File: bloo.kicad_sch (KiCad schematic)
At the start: 89 parts, among them J5 SWD_Header, M1 M1_Conn_Alt, M2 M2_Conn_Alt, Q0 TEFT4300, Q1 TEFT4300, Q10 Q_NMOS_GSD, Q11 Q_NMOS_GSD, Q12 Q_NMOS_GSD, Q2 TEFT4300, Q3 TEFT4300, Q9 Q_NMOS_GSD, SW1 SW, SW2 SW, SW3 SW, U1 YAAJ_BluePill_SWD_Breakout, U2 L293D, U3 LM1085-5.0, U4 APE8865Y5-33-HF-3, U5 BC832

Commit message: BOM Complete
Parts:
- BT1: LCSC Part # (none) -> C160262
- C1, C12, C13, C19, C4: LCSC Part # (none) -> C600013
- C10: LCSC Part # (none) -> C1952791
- C11, C9: LCSC Part # (none) -> C39127
- C14, C15, C17, C18, C20, C21, C3: LCSC Part # (none) -> C28322
- C16, C2: LCSC Part # (none) -> C1590882
- C25: LCSC Part # (none) -> C1846
- C5: LCSC Part # (none) -> C1590
- C6: LCSC Part # (none) -> C140782
- D0, D1, D2, D3: LCSC Part # (none) -> C2900370
- D4: LCSC Part # (none) -> C5879380
- D5: LCSC Part # (none) -> C2890404
- D6: LCSC Part # (none) -> C2293
- L1: LCSC Part # (none) -> C845121
- M1, M2: LCSC Part # (none) -> C144397
- Q0, Q1, Q2, Q3: LCSC Part # (none) -> C118301
- Q10, Q11, Q12, Q9: LCSC Part # (none) -> C5310967
- R1, R2, R3, R4: value 1.8k -> 1.8K; LCSC Part # (none) -> C22108
- R10: value 10k -> 10K; LCSC Part # (none) -> C2479071
- R11, R12, R13, R14, R15, R16, R24: LCSC Part # (none) -> C25664
- R19: LCSC Part # (none) -> C17985
- R20, R21: LCSC Part # (none) -> C17987
- R22: LCSC Part # (none) -> C18003
- R23, R9: LCSC Part # (none) -> C2479751
- R5, R6, R7, R8: value 35 -> 36; LCSC Part # (none) -> C18006
- S1: LCSC Part # (none) -> C6689036
- SW1, SW2, SW3, SW_RST1: LCSC Part # (none) -> C2801245
- U1: LCSC Part # (none) -> C22396880; now not fitted
- U2: LCSC Part # (none) -> C12340
- U3: LCSC Part # (none) -> C129950
- U4: value APE8865Y5-33-HF-3 -> NCP161ASN330T1G; LCSC Part # (none) -> C892187
- U5: now not fitted

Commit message: Started Reza's suggested changes
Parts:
- removed R11: 47K, Resistor_SMD:R_1206_3216Metric_Pad1.30x1.75mm_HandSolder, symbol Device:R
- removed SW1: SW, Button_Switch_SMD:SW_SPST_REED_CT05-XXXX-G1, symbol Switch:SW_Push
- added C22: 0.1uF, Capacitor_SMD:C_1206_3216Metric_Pad1.33x1.80mm_HandSolder, symbol Device:C
- added C7, C8: 12pF, symbol Device:C
- added D7, D9: 1SS389,L3F, Diode_SMD:D_SOD-523, symbol Diode:1N4148WT
- added R17: 47K, Resistor_SMD:R_1206_3216Metric_Pad1.30x1.75mm_HandSolder, symbol Device:R
- added Y1: ABS07-32.768KHZ-T, AS07-XTAL:XTAL_ABS07-32.768KHZ-T, symbol ABS07-XTAL:ABS07-32.768KHZ-T
- BT1: footprint Connector_PinSocket_2.54mm:PinSocket_1x02_P2.54mm_Vertical -> Connector_JST:JST_EH_B2B-EH-A_1x02_P2.50mm_Vertical
- U1, U5: now fitted
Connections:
- net BUTTON is gone; now on net BLE_SPI_MISO: U1.12 (PB4)
- net +3V3: now also M1.4 (Pin_4), M2.4 (Pin_4), R17.2; no longer M1.3 (Pin_3), M2.3 (Pin_3)
- net BLE_STATE: now also U5.D2 (P19); no longer U5.2 (P20/LED)
- net BT_RESET: now also C22.1, D9.2 (A), R17.1
- net EMIT_4: now also U1.22 (PC13); no longer U1.13 (PB5)
- net GND: now also C19.1, M1.1 (Pin_1), M2.1 (Pin_1), C22.2, C7.1, C8.1; no longer C19.2, M1.6 (Pin_6), M2.6 (Pin_6)
- net M1_ENC_A: now also M1.3 (Pin_3); no longer M2.4 (Pin_4)
- net M1_ENC_B: now also M1.2 (Pin_2); no longer M2.5 (Pin_5)
- net M1_OUT_1: now also M1.6 (Pin_6); no longer M2.1 (Pin_1)
- net M1_OUT_2: now also M1.5 (Pin_5); no longer M2.2 (Pin_2)
- net M2_ENC_A: now also M2.3 (Pin_3); no longer M1.4 (Pin_4)
- net M2_ENC_B: now also M2.2 (Pin_2); no longer M1.5 (Pin_5)
- net M2_OUT_1: now also M2.6 (Pin_6); no longer M1.1 (Pin_1)
- net M2_OUT_2: now also M2.5 (Pin_5); no longer M1.2 (Pin_2)
- net RST: now also C19.2, D7.2 (A); no longer C19.1, SW_RST1.1
- net BLE_SPI_SCK: now reaches U1.11 (PB3)
- net BLE_SPI_SCK: now also U5.A5 (P08)
- net BLE_LED: now reaches U1.24 (PC15)
- net BLE_LED: now also U5.A2 (P17)
- net at U5.11 (P00/XL1): now also C8.2, Y1.1
- net at U5.12 (P01/XL2): now also C7.2, Y1.2
- net BLE_SPI_MISO: now reaches U5.C5 (P09)
- net BLE_SPI_MOSI: now reaches U5.D5 (P10)
- net BLE_SPI_MOSI: now also U1.13 (PB5)
- new net: D7.1 (K), D9.1 (K), SW_RST1.1
- no-connect marks 32 -> 24
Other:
- moved on the sheet: C19, J5, M1, M2, R12, R24, R9, SW2, SW3, SW_RST1

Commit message: updated button footprint
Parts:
- SW3: footprint Button_Switch_SMD:SW_SPST_REED_CT05-XXXX-G1 -> MM_Library:SW4_SKRPABE010_ALPS
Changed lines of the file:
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@@
 			)
 		)
-		(property "Footprint" "Button_Switch_SMD:SW_SPST_REED_CT05-XXXX-G1"
+		(property "Footprint" "MM_Library:SW4_SKRPABE010_ALPS"
 			(at 46.355 252.73 0)
 			(effects

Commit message: reorganized schematics
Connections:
- net BUTTON_3 is gone; now on net BUTTON_2: R9.2, SW3.1, U1.17 (PB9)
- net BUTTON_2: no longer R24.2, SW2.1, U1.23 (PC14)
- new net BUTTON: R24.2, SW2.1, U1.23 (PC14)
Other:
- note added: "Buttons"
- note added: "LEDs"
- note removed: "Button, LEDs"
- moved on the sheet: BT1, BT_MH1, BT_MH2, BT_MH3, BT_MH4, C1, C10, C11, C12, C13, C14, C15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

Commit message: updated pcb from schematics
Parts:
- C7, C8: footprint (none) -> Capacitor_SMD:C_0603_1608Metric_Pad1.08x0.95mm_HandSolder
- Y1: footprint AS07-XTAL:XTAL_ABS07-32.768KHZ-T -> MM_Library:CAP_ABS07-32.768KHZ-T_ABR
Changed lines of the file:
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@@
 			)
 		)
-		(property "Footprint" ""
+		(property "Footprint" "Capacitor_SMD:C_0603_1608Metric_Pad1.08x0.95mm_HandSolder"
 			(at 295.91 137.4648 0)
 			(effects
@@
 			)
 		)
-		(property "Footprint" ""
+		(property "Footprint" "Capacitor_SMD:C_0603_1608Metric_Pad1.08x0.95mm_HandSolder"
 			(at 295.91 124.7648 0)
 			(effects
@@
 			)
 		)
-		(property "Footprint" "AS07-XTAL:XTAL_ABS07-32.768KHZ-T"
+		(property "Footprint" "MM_Library:CAP_ABS07-32.768KHZ-T_ABR"
 			(at 299.72 132.08 0)
 			(effects

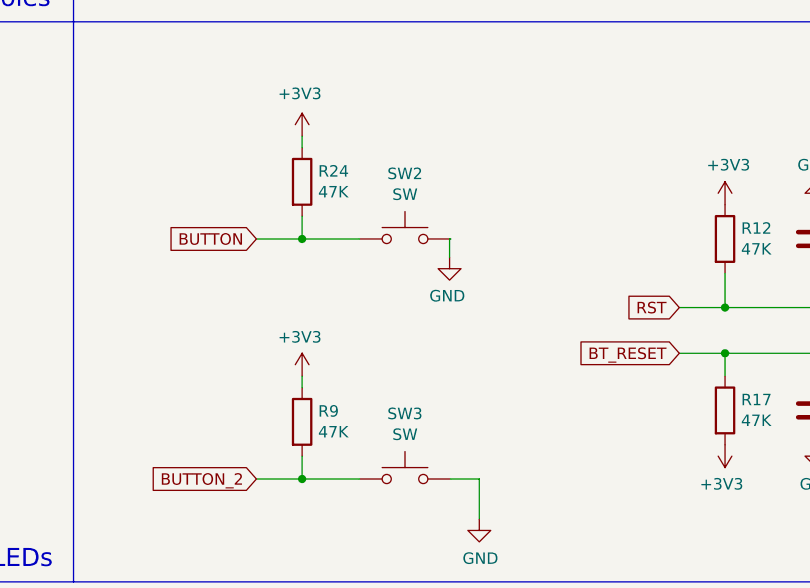
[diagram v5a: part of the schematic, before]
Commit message: updated buttons in pcb
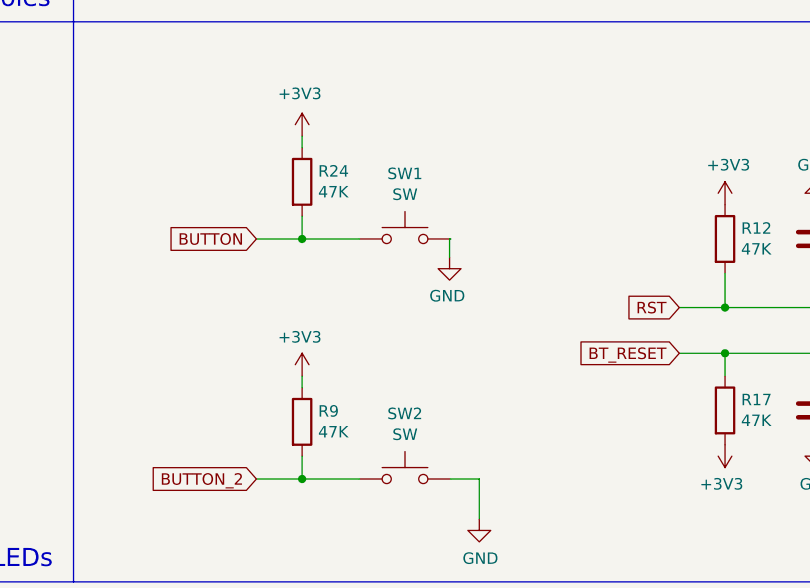
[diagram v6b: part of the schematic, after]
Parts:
- SW1: renamed from SW2; footprint Button_Switch_SMD:SW_SPST_REED_CT05-XXXX-G1 -> MM_Library:SW4_SKRPABE010_ALPS
- SW_RST1: footprint Button_Switch_SMD:SW_SPST_REED_CT05-XXXX-G1 -> MM_Library:SW4_SKRPABE010_ALPS
- U5: footprint custom_foot:XCVR_BC832 -> MM_Library:XCVR_BC832
- renumbered SW3 to SW2
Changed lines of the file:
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@@
 			)
 		)
-		(property "Footprint" "Button_Switch_SMD:SW_SPST_REED_CT05-XXXX-G1"
+		(property "Footprint" "MM_Library:SW4_SKRPABE010_ALPS"
 			(at 388.62 212.09 0)
 			(effects
@@
 		(on_board yes)
 		(dnp no)
-		(property "Reference" "SW2"
+		(property "Reference" "SW1"
 			(at 303.53 202.311 0)
 			(effects
@@
 			)
 		)
-		(property "Footprint" "Button_Switch_SMD:SW_SPST_REED_CT05-XXXX-G1"
+		(property "Footprint" "MM_Library:SW4_SKRPABE010_ALPS"
 			(at 303.53 204.47 0)
 			(effects
@@
 			(project "bloo"
 				(path "/9031bb33-c6aa-4758-bf5c-3274ed3ebab7"
-					(reference "SW2")
+					(reference "SW1")
 					(unit 1)
 				)
@@
 			)
 		)
-		(property "Footprint" "custom_foot:XCVR_BC832"
+		(property "Footprint" "MM_Library:XCVR_BC832"
 			(at 347.98 146.05 0)
 			(effects
@@
 		(on_board yes)
 		(dnp no)
-		(property "Reference" "SW3"
+		(property "Reference" "SW2"
 			(at 303.53 228.981 0)
 			(effects
@@
 			(project "bloo"
 				(path "/9031bb33-c6aa-4758-bf5c-3274ed3ebab7"
-					(reference "SW3")
+					(reference "SW2")
 					(unit 1)
 				)

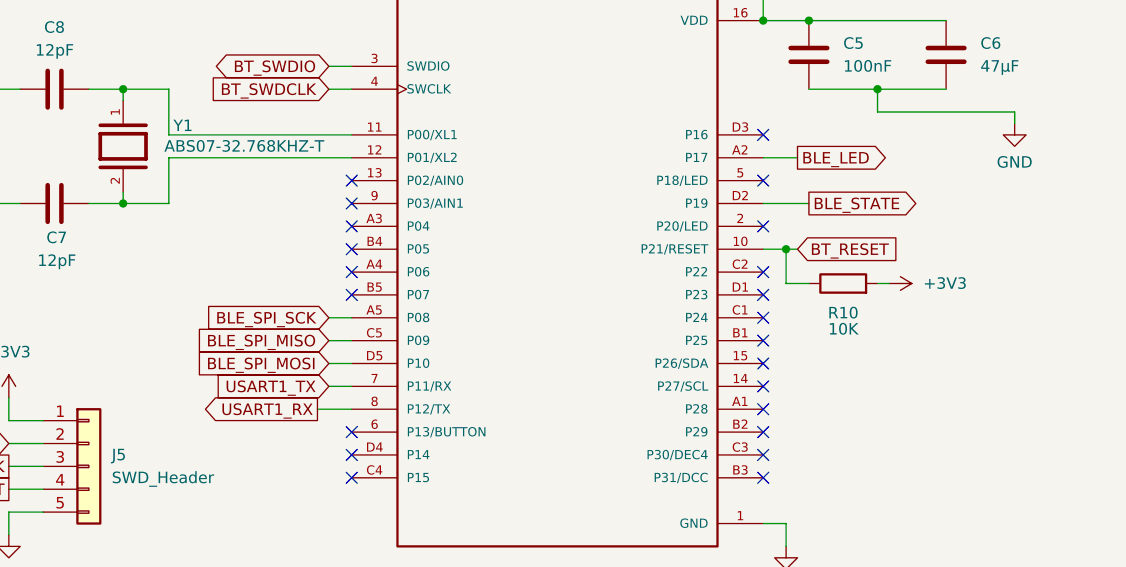
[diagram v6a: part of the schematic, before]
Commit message: change bluetooth SPI pins
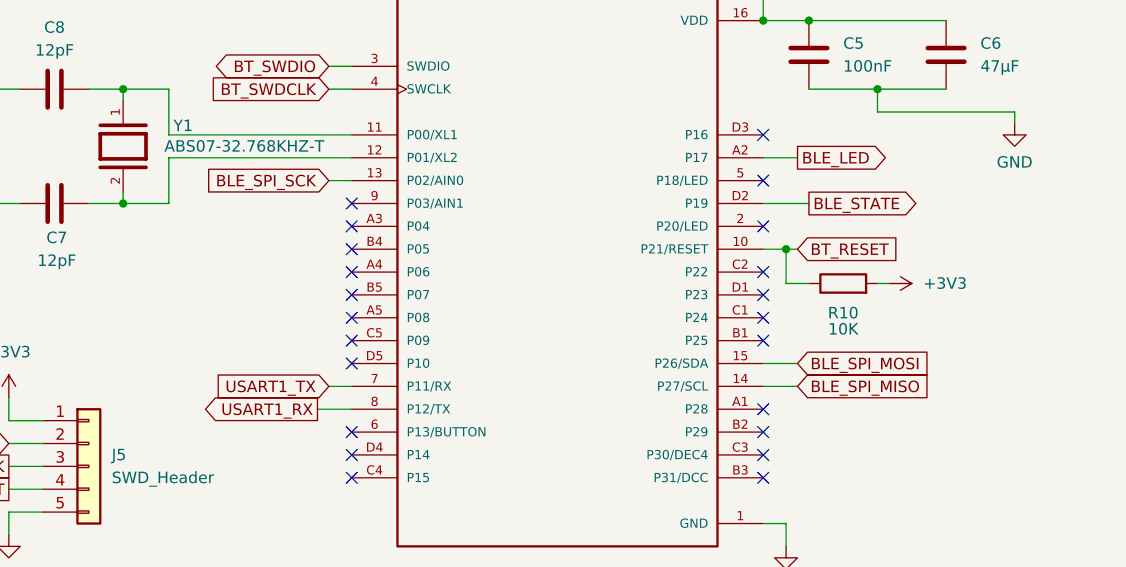
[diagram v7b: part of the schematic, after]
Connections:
- net BLE_SPI_MISO: now also U5.14 (P27/SCL); no longer U5.C5 (P09)
- net BLE_SPI_MOSI: now also U5.15 (P26/SDA); no longer U5.D5 (P10)
- net BLE_SPI_SCK: now also U5.13 (P02/AIN0); no longer U5.A5 (P08)
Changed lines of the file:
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@@
 	)
 	(no_connect
-		(at 370.84 156.21)
-	)
-	(no_connect
 		(at 325.12 143.51)
 	)
 	(no_connect
-		(at 325.12 135.89)
-	)
-	(no_connect
 		(at 218.44 48.26)
 	)
@@
 	)
 	(no_connect
+		(at 325.12 156.21)
+	)
+	(no_connect
 		(at 325.12 140.97)
 	)
 	(no_connect
+		(at 325.12 153.67)
+	)
+	(no_connect
 		(at 370.84 153.67)
 	)
@@
 	)
 	(no_connect
-		(at 370.84 168.91)
+		(at 325.12 151.13)
 	)
 	(no_connect
-		(at 370.84 146.05)
+		(at 370.84 168.91)
 	)
 	(no_connect
-		(at 370.84 158.75)
+		(at 370.84 146.05)
 	)
 	(no_connect
@@
 	(wire
 		(pts
+			(xy 374.65 158.75) (xy 370.84 158.75)
+		)
+		(stroke
+			(width 0)
+			(type default)
+		)
+	)
+	(wire
+		(pts
 			(xy 91.948 98.679) (xy 115.57 98.679)
 		)
@@
 	(wire
 		(pts
+			(xy 374.65 156.21) (xy 370.84 156.21)
+		)
+		(stroke
+			(width 0)
+			(type default)
+		)
+	)
+	(wire
+		(pts
 			(xy 236.22 235.585) (xy 229.235 235.585)
 		)
@@
 	(wire
 		(pts
+			(xy 322.58 135.89) (xy 325.12 135.89)
+		)
+		(stroke
+			(width 0)
+			(type default)
+		)
+	)
+	(wire
+		(pts
 			(xy 241.3 60.96) (xy 245.11 60.96)
 		)
@@
 	(wire
 		(pts
-			(xy 322.58 156.21) (xy 325.12 156.21)
-		)
-		(stroke
-			(width 0)
-			(type default)
-		)
-	)
-	(wire
-		(pts
 			(xy 373.38 147.32) (xy 375.92 147.32)
 		)
@@
 		)
 	)
-	(wire
-		(pts
-			(xy 322.58 151.13) (xy 325.12 151.13)
-		)
-		(stroke
-			(width 0)
-			(type default)
-		)
-	)
 	(polyline
 		(pts
@@
 	(wire
 		(pts
-			(xy 322.58 153.67) (xy 325.12 153.67)
-		)
-		(stroke
-			(width 0)
-			(type default)
-		)
-	)
-	(wire
-		(pts
 			(xy 47.879 113.919) (xy 47.879 116.713)
 		)
@@
 	(global_label "BLE_SPI_MOSI"
 		(shape input)
-		(at 322.58 156.21 180)
+		(at 374.65 156.21 0)
 		(fields_autoplaced yes)
 		(effects
@@
 				(size 1.27 1.27)
 			)
-			(justify right)
+			(justify left)
 		)
 		(property "Intersheetrefs" "${INTERSHEET_REFS}"
-			(at 307.1862 156.21 0)
+			(at 390.0438 156.21 0)
 			(effects
 				(font
 					(size 1.27 1.27)
 				)
-				(justify right)
+				(justify left)
 				(hide yes)
 			)
@@
 	(global_label "BLE_SPI_MISO"
 		(shape input)
-		(at 322.58 153.67 180)
+		(at 374.65 158.75 0)
 		(fields_autoplaced yes)
 		(effects
@@
 				(size 1.27 1.27)
 			)
-			(justify right)
+			(justify left)
 		)
 		(property "Intersheetrefs" "${INTERSHEET_REFS}"
-			(at 307.1862 153.67 0)
+			(at 390.0438 158.75 0)
 			(effects
 				(font
 					(size 1.27 1.27)
 				)
-				(justify right)
+				(justify left)
 				(hide yes)
 			)
@@
 	(global_label "BLE_SPI_SCK"
 		(shape input)
-		(at 322.58 151.13 180)
+		(at 322.58 135.89 180)
 		(fields_autoplaced yes)
 		(effects
@@
 		)
 		(property "Intersheetrefs" "${INTERSHEET_REFS}"
-			(at 308.0329 151.13 0)
+			(at 308.0329 135.89 0)
 			(effects
 				(font

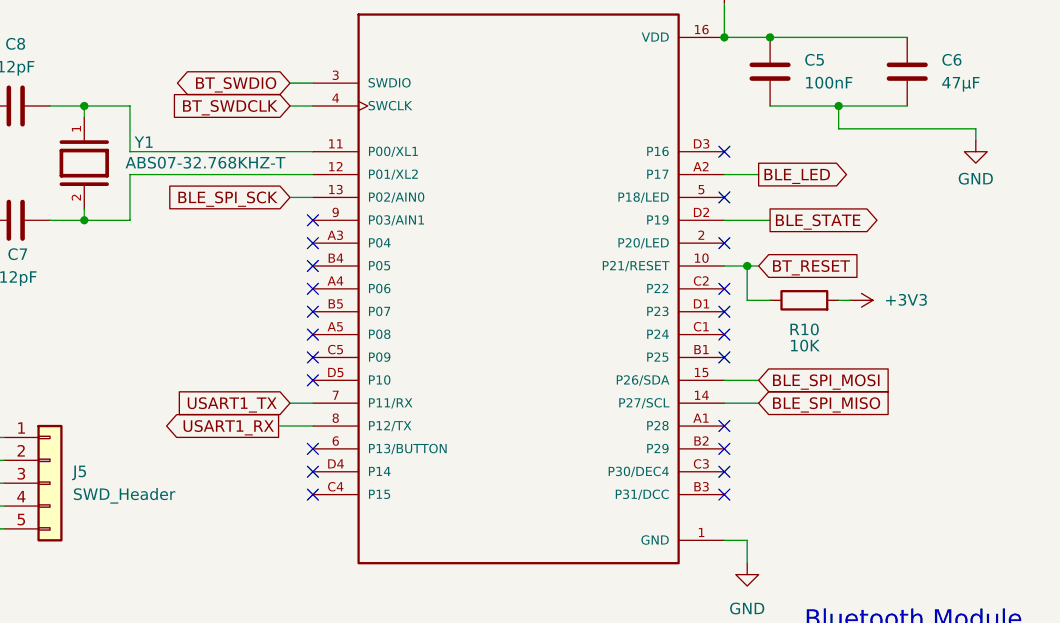
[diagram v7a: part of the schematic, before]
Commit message: rerouted LED/State to edge pins on BLE
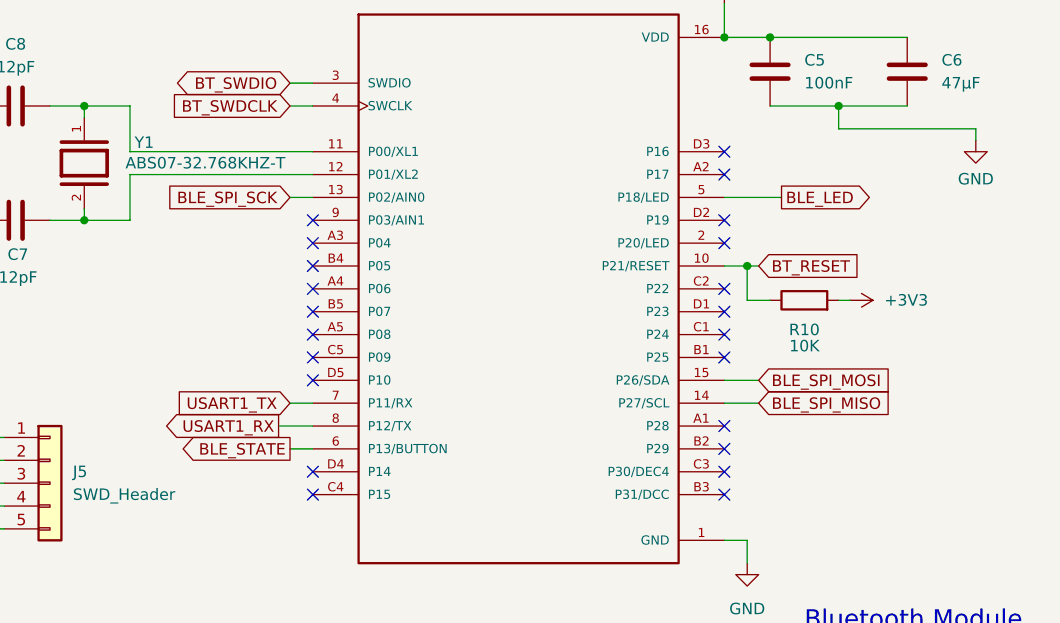
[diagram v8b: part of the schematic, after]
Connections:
- net BLE_LED: now also U5.5 (P18/LED); no longer U5.A2 (P17)
- net BLE_STATE: now also U5.6 (P13/BUTTON); no longer U5.D2 (P19)
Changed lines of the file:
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@@
 	)
 	(no_connect
+		(at 370.84 138.43)
+	)
+	(no_connect
 		(at 218.44 48.26)
 	)
@@
 	)
 	(no_connect
-		(at 370.84 135.89)
-	)
-	(no_connect
-		(at 325.12 163.83)
-	)
-	(no_connect
 		(at 325.12 146.05)
 	)
@@
 	)
 	(no_connect
+		(at 370.84 133.35)
+	)
+	(no_connect
 		(at 370.84 130.81)
 	)
@@
 	(wire
 		(pts
+			(xy 377.19 135.89) (xy 370.84 135.89)
+		)
+		(stroke
+			(width 0)
+			(type default)
+		)
+	)
+	(wire
+		(pts
 			(xy 109.855 252.095) (xy 109.855 254)
 		)
@@
 	(wire
 		(pts
-			(xy 375.92 138.43) (xy 370.84 138.43)
-		)
-		(stroke
-			(width 0)
-			(type default)
-		)
-	)
-	(wire
-		(pts
 			(xy 82.042 52.451) (xy 76.327 52.451)
 		)
@@
 	(wire
 		(pts
-			(xy 66.675 227.33) (xy 66.675 231.14)
+			(xy 322.58 163.83) (xy 325.12 163.83)
 		)
 		(stroke
@@
 	(wire
 		(pts
-			(xy 330.2 64.77) (xy 331.47 64.77)
+			(xy 66.675 227.33) (xy 66.675 231.14)
 		)
 		(stroke
@@
 	(wire
 		(pts
-			(xy 374.65 133.35) (xy 370.84 133.35)
+			(xy 330.2 64.77) (xy 331.47 64.77)
 		)
 		(stroke
@@
 	(global_label "BLE_LED"
 		(shape output)
-		(at 374.65 133.35 0)
+		(at 377.19 135.89 0)
 		(fields_autoplaced yes)
 		(effects
@@
 		)
 		(property "Intersheetrefs" "${INTERSHEET_REFS}"
-			(at 384.8428 133.35 0)
+			(at 387.3828 135.89 0)
 			(effects
 				(font
@@
 		)
 	)
+	(global_label "BLE_STATE"
+		(shape output)
+		(at 322.58 163.83 180)
+		(fields_autoplaced yes)
+		(effects
+			(font
+				(size 1.27 1.27)
+			)
+			(justify right)
+		)
+		(property "Intersheetrefs" "${INTERSHEET_REFS}"
+			(at 310.452 163.83 0)
+			(effects
+				(font
+					(size 1.27 1.27)
+				)
+				(justify right)
+				(hide yes)
+			)
+		)
+	)
 	(global_label "M1_OUT_2"
 		(shape input)
@@
 				(hide yes)
 			)
-		)
-	)
-	(global_label "BLE_STATE"
-		(shape output)
-		(at 375.92 138.43 0)
-		(fields_autoplaced yes)
-		(effects
-			(font
-				(size 1.27 1.27)
-			)
-			(justify left)
-		)
-		(property "Intersheetrefs" "${INTERSHEET_REFS}"
-			(at 388.048 138.43 0)
-			(effects
-				(font
-					(size 1.27 1.27)
-				)
-				(justify left)
-				(hide yes)
-			)
